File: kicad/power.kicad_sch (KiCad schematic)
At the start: 30 parts, among them J1 12V IN, Q10 AOD4185, U1 TPS54360B, U2 AMS1117-3.3

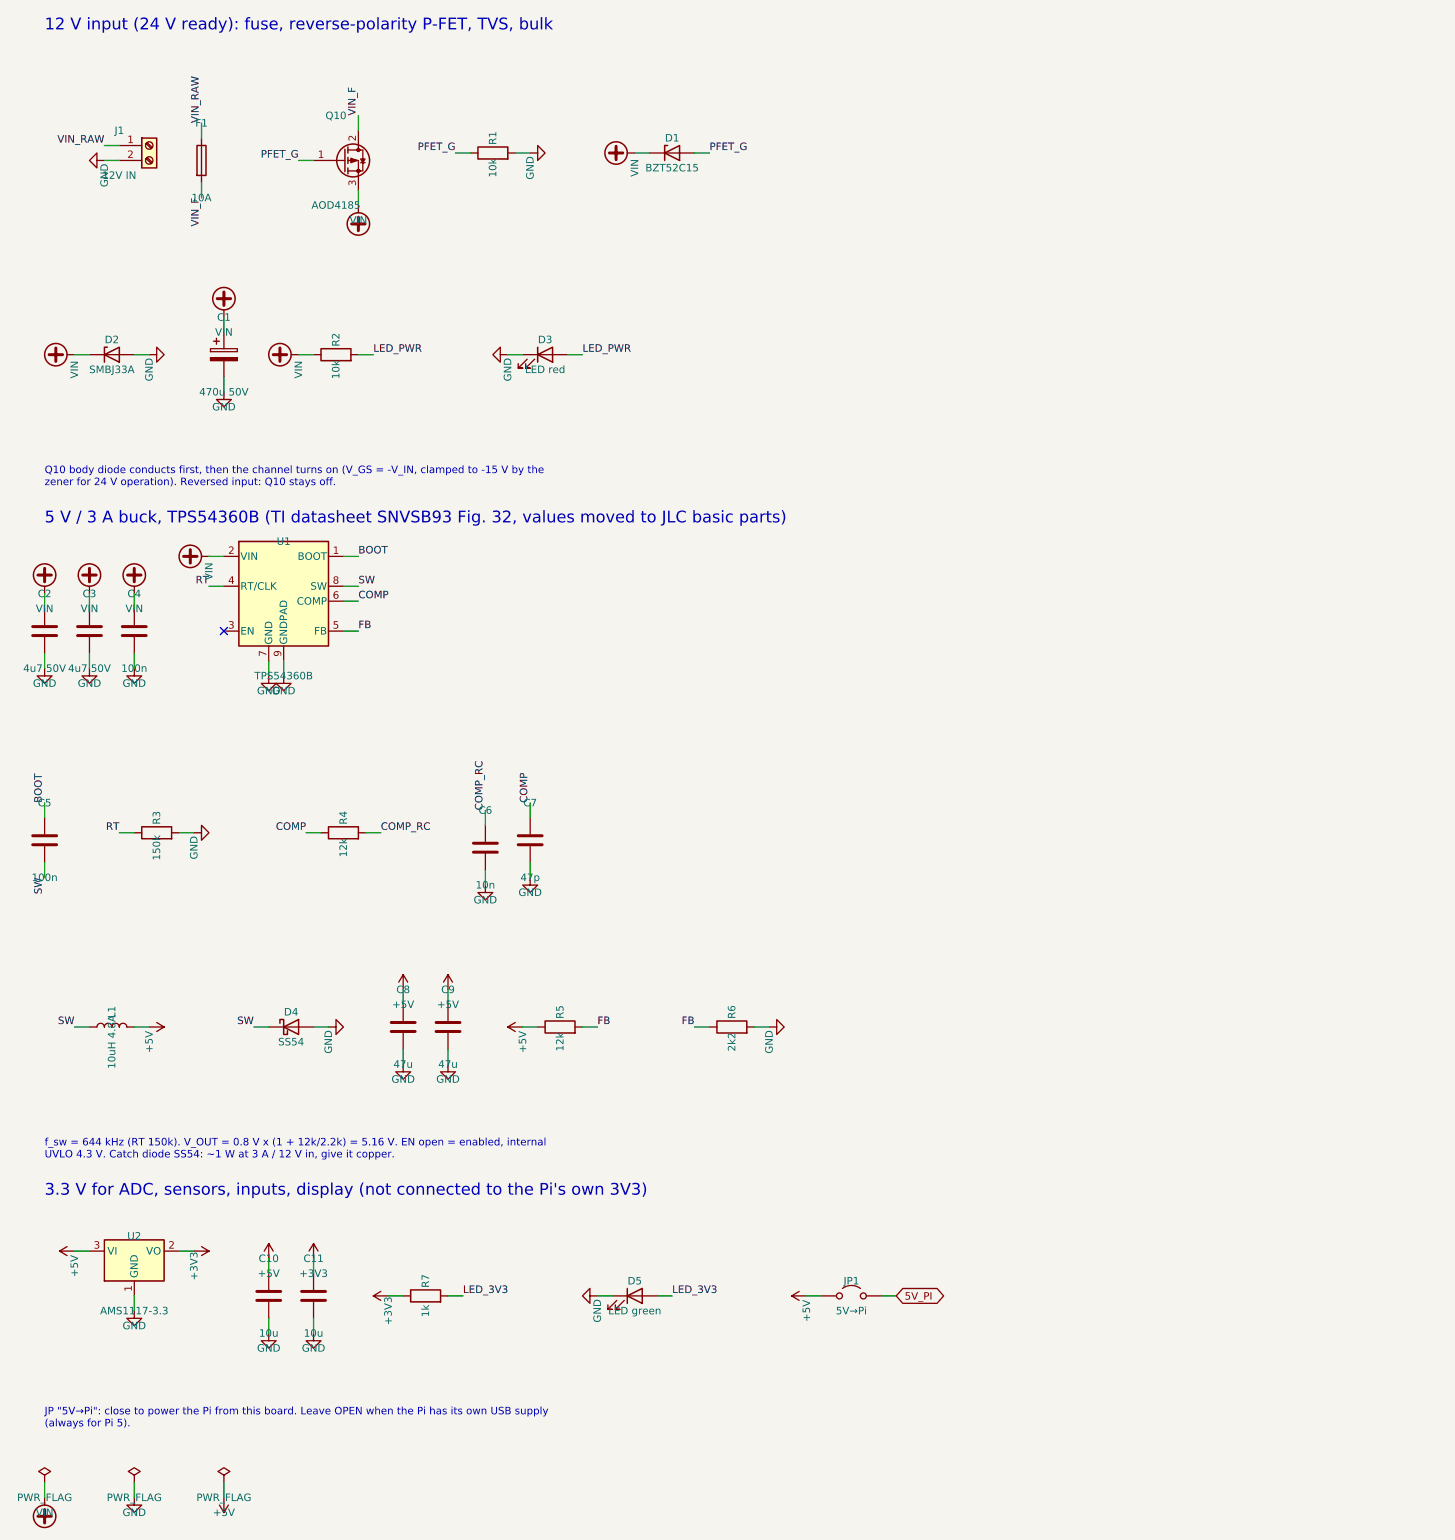
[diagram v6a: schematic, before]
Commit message: kicad: restore the hand-edited schematic from KiCad local history
f617249 overwrote the schematic that had been tidied by hand in
eeschema (labels replaced by wires and junctions) with a regenerated
draft and new symbol UUIDs. Restore all sheets and the project file
from KiCad's local history snapshot eb84d42 (2026-09-30 14:45).
Connectivity matches that snapshot; all 153 symbols link to the
footprints in aquaPCB.kicad_pcb again. The third 1-Wire terminal (J21)
is still in the schematic and has to be deleted in eeschema.

Co-Authored-By: Claude Opus 5.5 <noreply@anthropic.com>
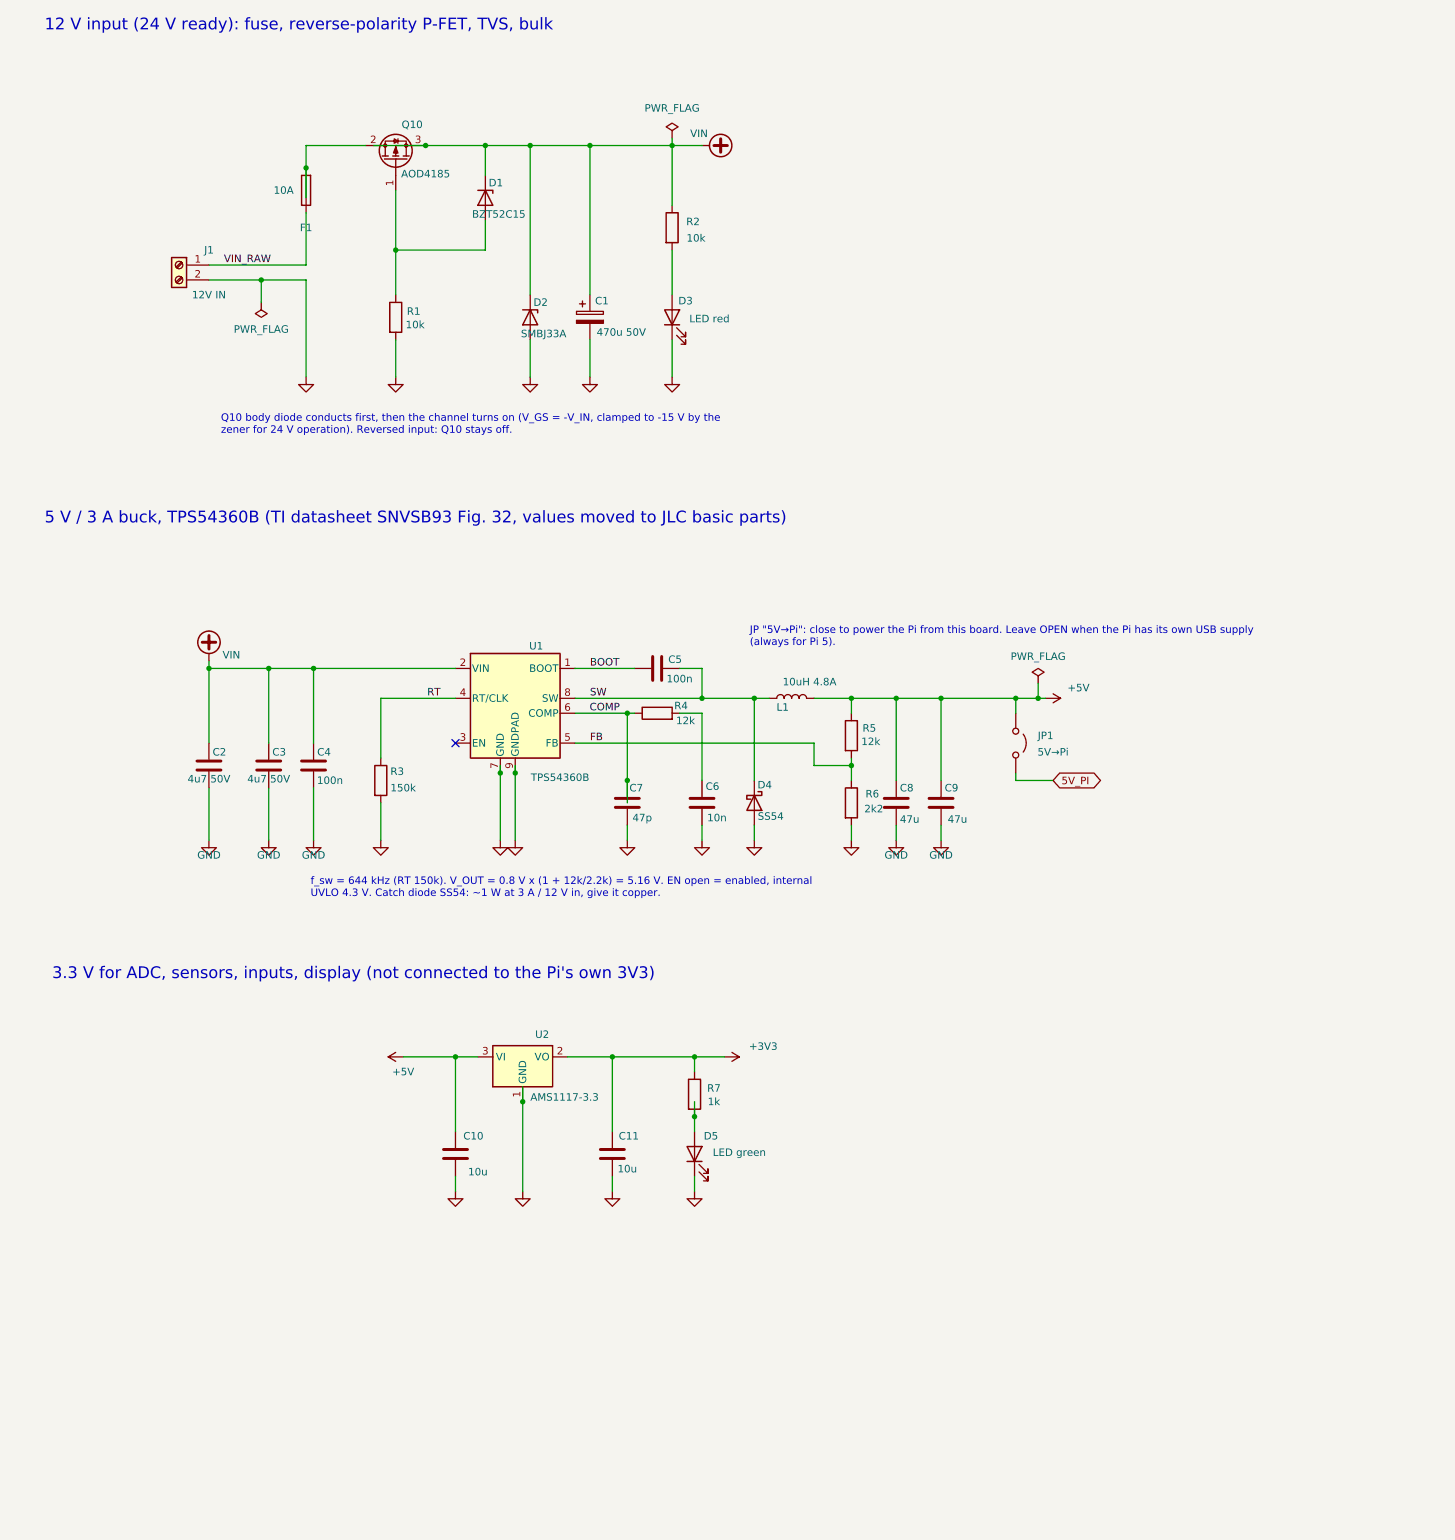
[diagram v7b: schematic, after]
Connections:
- net COMP_RC: no longer names the net of C6.1, R4.2
- net LED_3V3: no longer names the net of D5.2 (A), R7.2
- net LED_PWR: no longer names the net of D3.2 (A), R2.2
- net PFET_G: no longer names the net of D1.2 (A), Q10.1 (G), R1.1
- net VIN_F: no longer names the net of F1.2, Q10.2 (D)

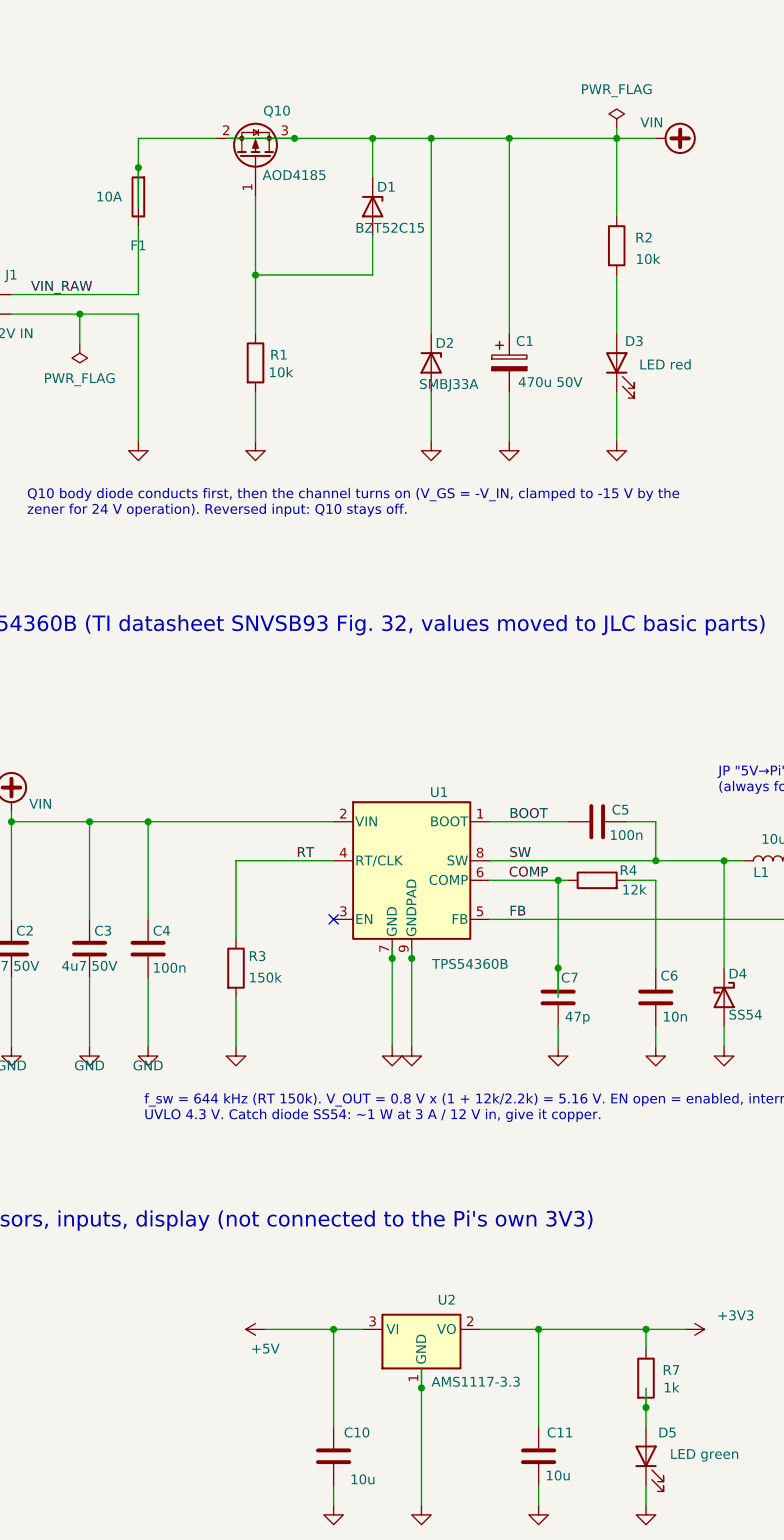
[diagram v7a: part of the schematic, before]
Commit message: kicad: fix connections broken while tidying the schematic
analog: AIN1 (U5.5) reconnected to PH_REF, AIN2 and AIN3 filter nodes
reconnected to their clamps / ADC inputs (net labels), two dangling
wire pieces removed. power: seven dangling wire stubs removed.
ERC clean; connectivity equals the design of 7b8e8dd except the removed
J21 and the (equivalent) swapped JP3 pins. Minimal text edits, the rest
of the hand-edited drawing is untouched.

Co-Authored-By: Claude Opus 5.5 <noreply@anthropic.com>
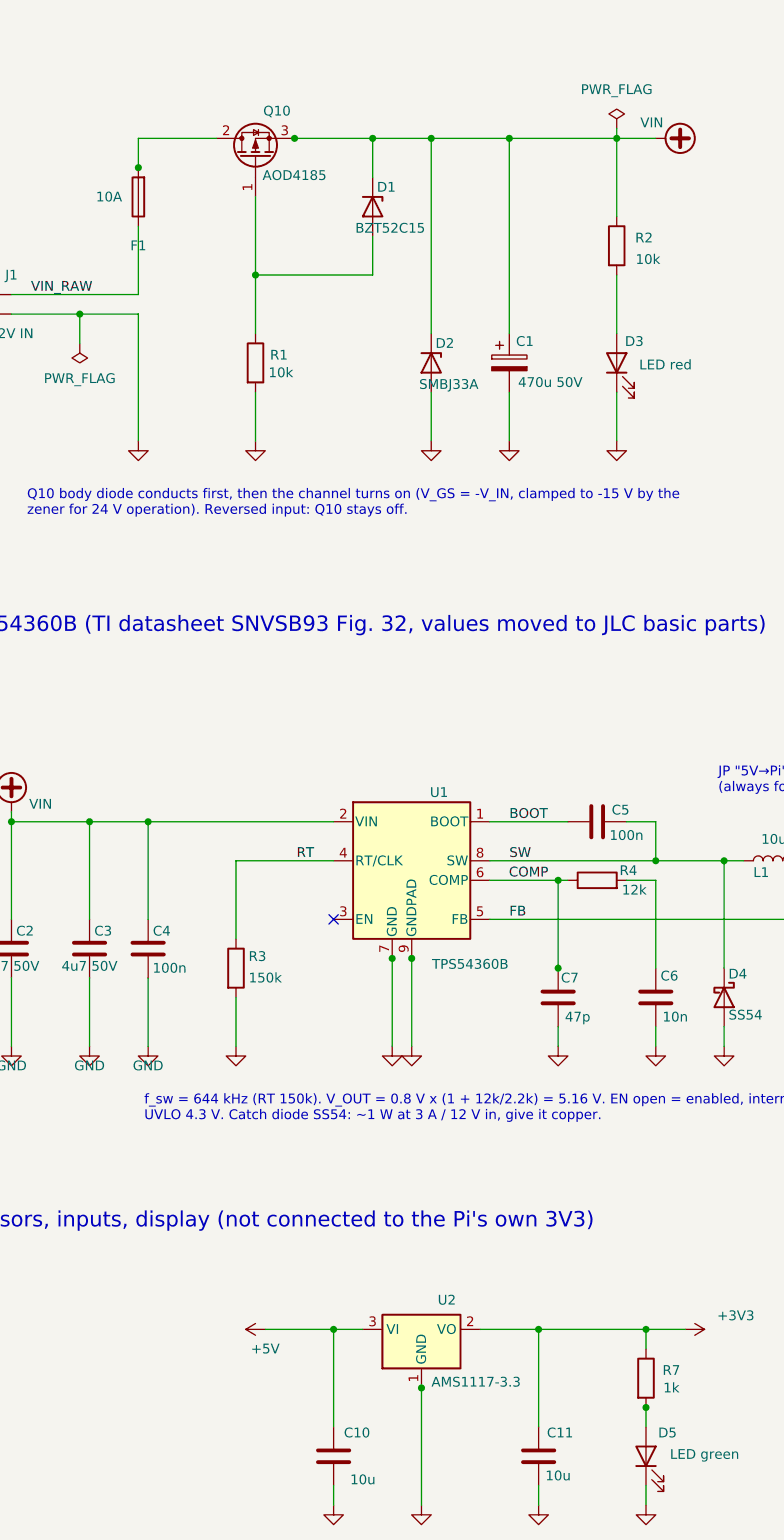
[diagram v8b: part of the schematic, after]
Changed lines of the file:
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@@
-	(wire
-		(pts
-			(xy 106.68 212.09) (xy 106.68 214.63)
-		)
-		(stroke
-			(width 0)
-			(type default)
-		)
-	)
 	(wire
 		(pts
@@
 	(wire
 		(pts
-			(xy 105.41 157.48) (xy 105.41 158.75)
-		)
-		(stroke
-			(width 0)
-			(type default)
-		)
-	)
-	(wire
-		(pts
 			(xy 135.89 209.55) (xy 135.89 207.01)
 		)
@@
 	(wire
 		(pts
-			(xy 135.89 214.63) (xy 135.89 217.17)
-		)
-		(stroke
-			(width 0)
-			(type default)
-		)
-	)
-	(wire
-		(pts
 			(xy 196.85 160.02) (xy 190.5 160.02)
 		)
@@
 	(wire
 		(pts
-			(xy 69.85 60.96) (xy 69.85 55.88)
-		)
-		(stroke
-			(width 0)
-			(type default)
-		)
-	)
-	(wire
-		(pts
 			(xy 118.11 52.07) (xy 132.08 52.07)
 		)
@@
 	(wire
 		(pts
-			(xy 124.46 160.02) (xy 124.46 163.83)
-		)
-		(stroke
-			(width 0)
-			(type default)
-		)
-	)
-	(wire
-		(pts
 			(xy 132.08 85.09) (xy 132.08 91.44)
 		)
@@
 	(wire
 		(pts
-			(xy 81.28 52.07) (xy 90.17 52.07)
-		)
-		(stroke
-			(width 0)
-			(type default)
-		)
-	)
-	(wire
-		(pts
 			(xy 194.31 143.51) (xy 194.31 146.05)
 		)
 		(stroke
-			(width 0)
-			(type default)
-		)
-	)
-	(wire
-		(pts
-			(xy 102.87 157.48) (xy 102.87 158.75)
-		)
-		(stroke
